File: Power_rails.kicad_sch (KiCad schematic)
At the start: 73 parts

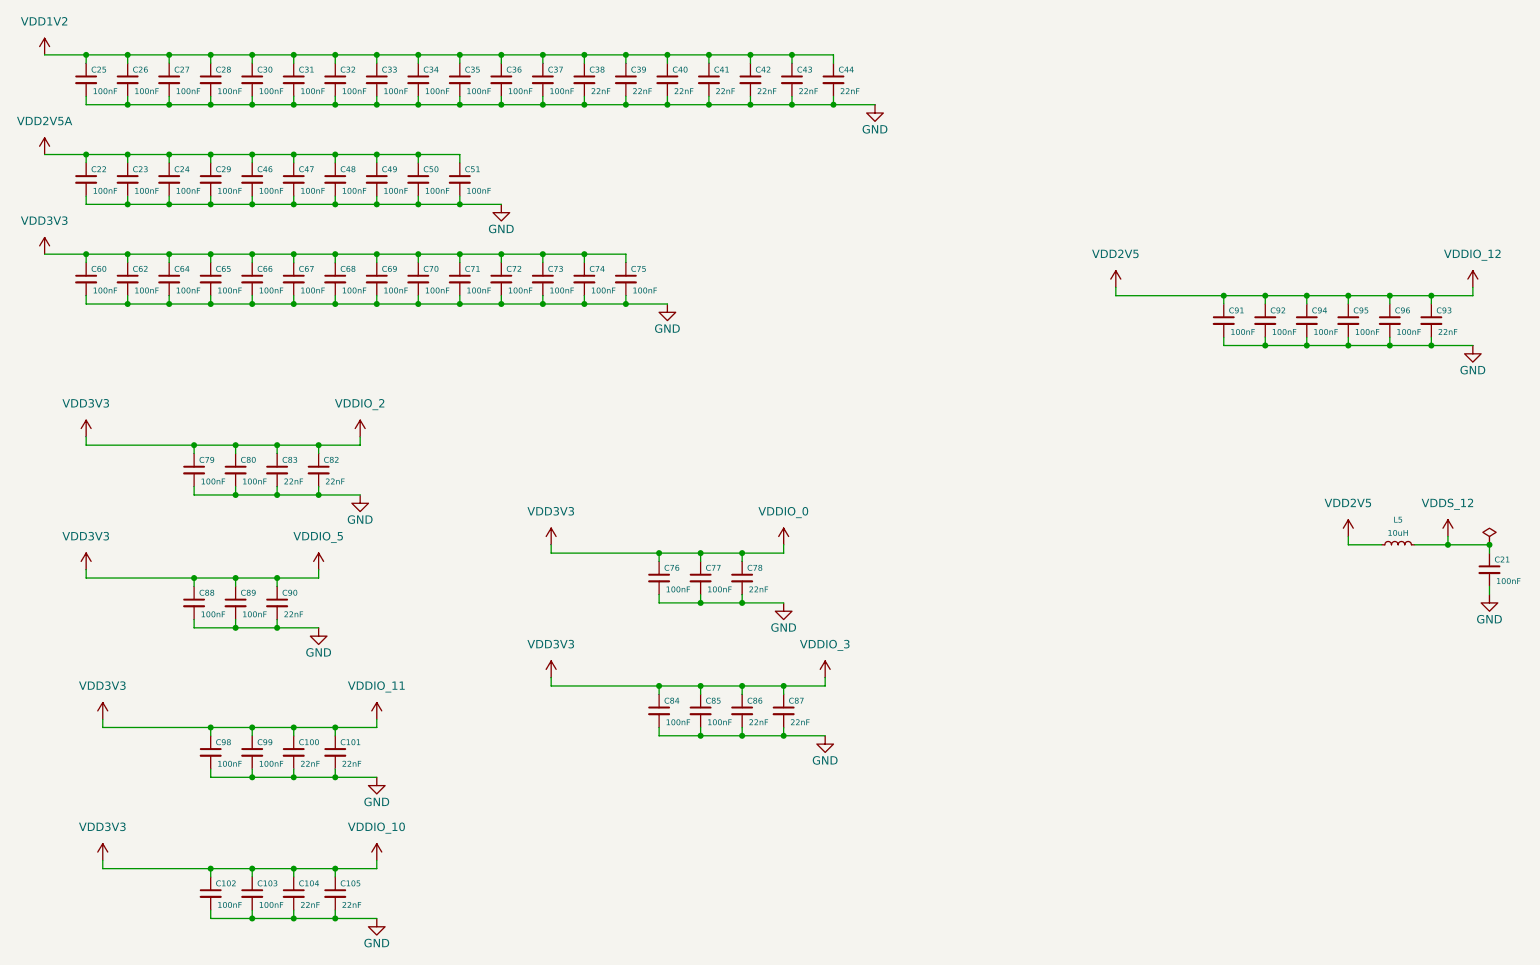
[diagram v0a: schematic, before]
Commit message: pre-order adjustments
DF9 connectors footprint adjusted.
Dimensions of board edges changed.
Placement of DF9 adjusted.
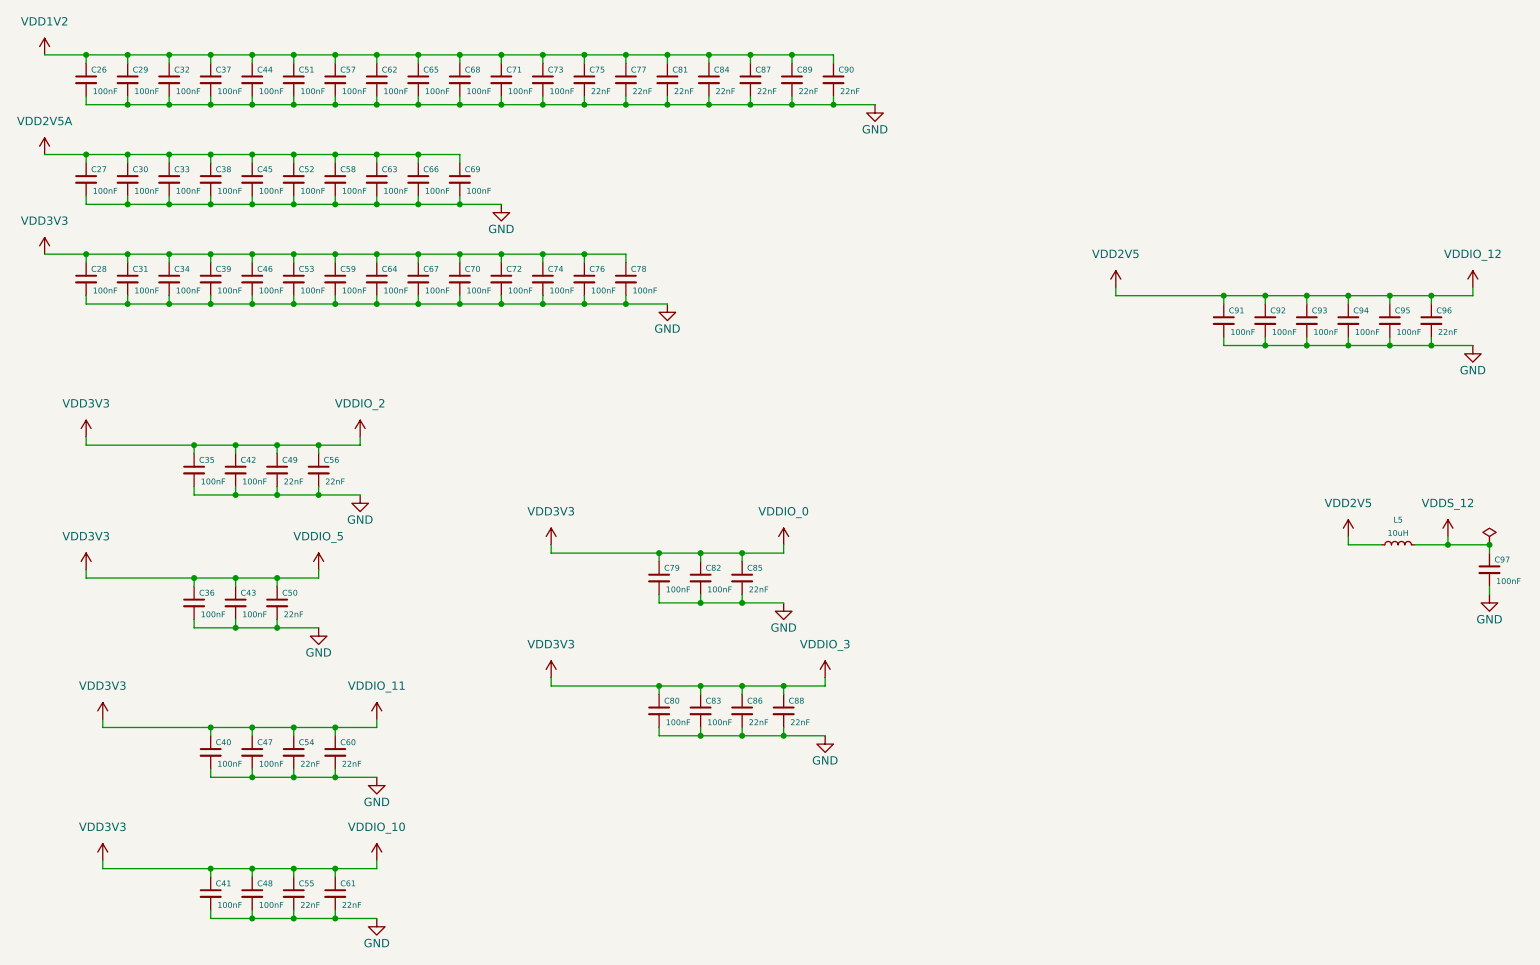
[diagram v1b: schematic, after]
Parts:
- renumbered C25 to C26, C22 to C27, C60 to C28, C26 to C29, C23 to C30, C62 to C31, C27 to C32, C24 to C33, C64 to C34, C79 to C35, C88 to C36, C28 to C37, C29 to C38, C65 to C39, C98 to C40, C102 to C41, C80 to C42, C89 to C43, C30 to C44, C46 to C45, C66 to C46, C99 to C47, C103 to C48, C83 to C49, C90 to C50, C31 to C51, C47 to C52, C67 to C53, C100 to C54, C104 to C55, C82 to C56, C32 to C57, C48 to C58, C68 to C59, C101 to C60, C105 to C61, C33 to C62, C49 to C63, C69 to C64, C34 to C65, C50 to C66, C70 to C67, C35 to C68, C51 to C69, C71 to C70, C36 to C71, C37 to C73, C73 to C74, C38 to C75, C74 to C76, C39 to C77, C75 to C78, C76 to C79, C84 to C80, C40 to C81, C77 to C82, C85 to C83, C41 to C84, C78 to C85, C42 to C87, C87 to C88, C43 to C89, C44 to C90, C94 to C93, C95 to C94, C96 to C95, C93 to C96, C21 to C97

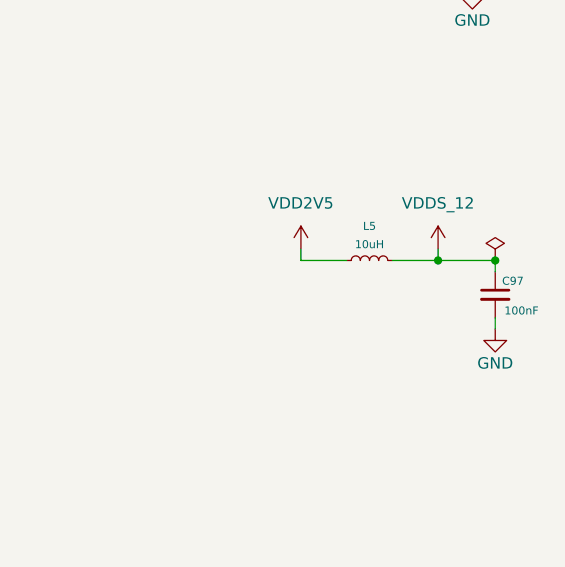
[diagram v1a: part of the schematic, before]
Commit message: pre order adjustments. Board symmetry
adjusted little things brought up by DFM checker of JLCPCB. Board's edges fully symmetrical on y axis. 2mm shift on x axis of the DF9s maintained
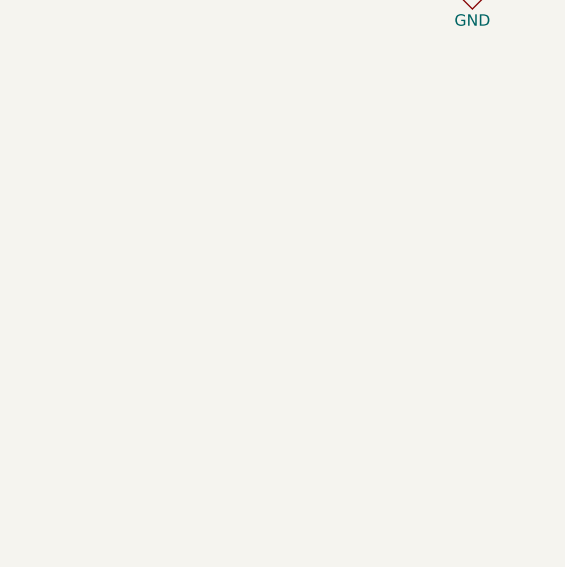
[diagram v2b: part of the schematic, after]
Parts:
- removed C97: 100nF, Capacitor_SMD:C_0402_1005Metric_Pad0.74x0.62mm_HandSolder, symbol Device:C_Small
- removed L5: 10uH, Inductor_SMD:L_0402_1005Metric_Pad0.77x0.64mm_HandSolder, symbol Device:L_Small

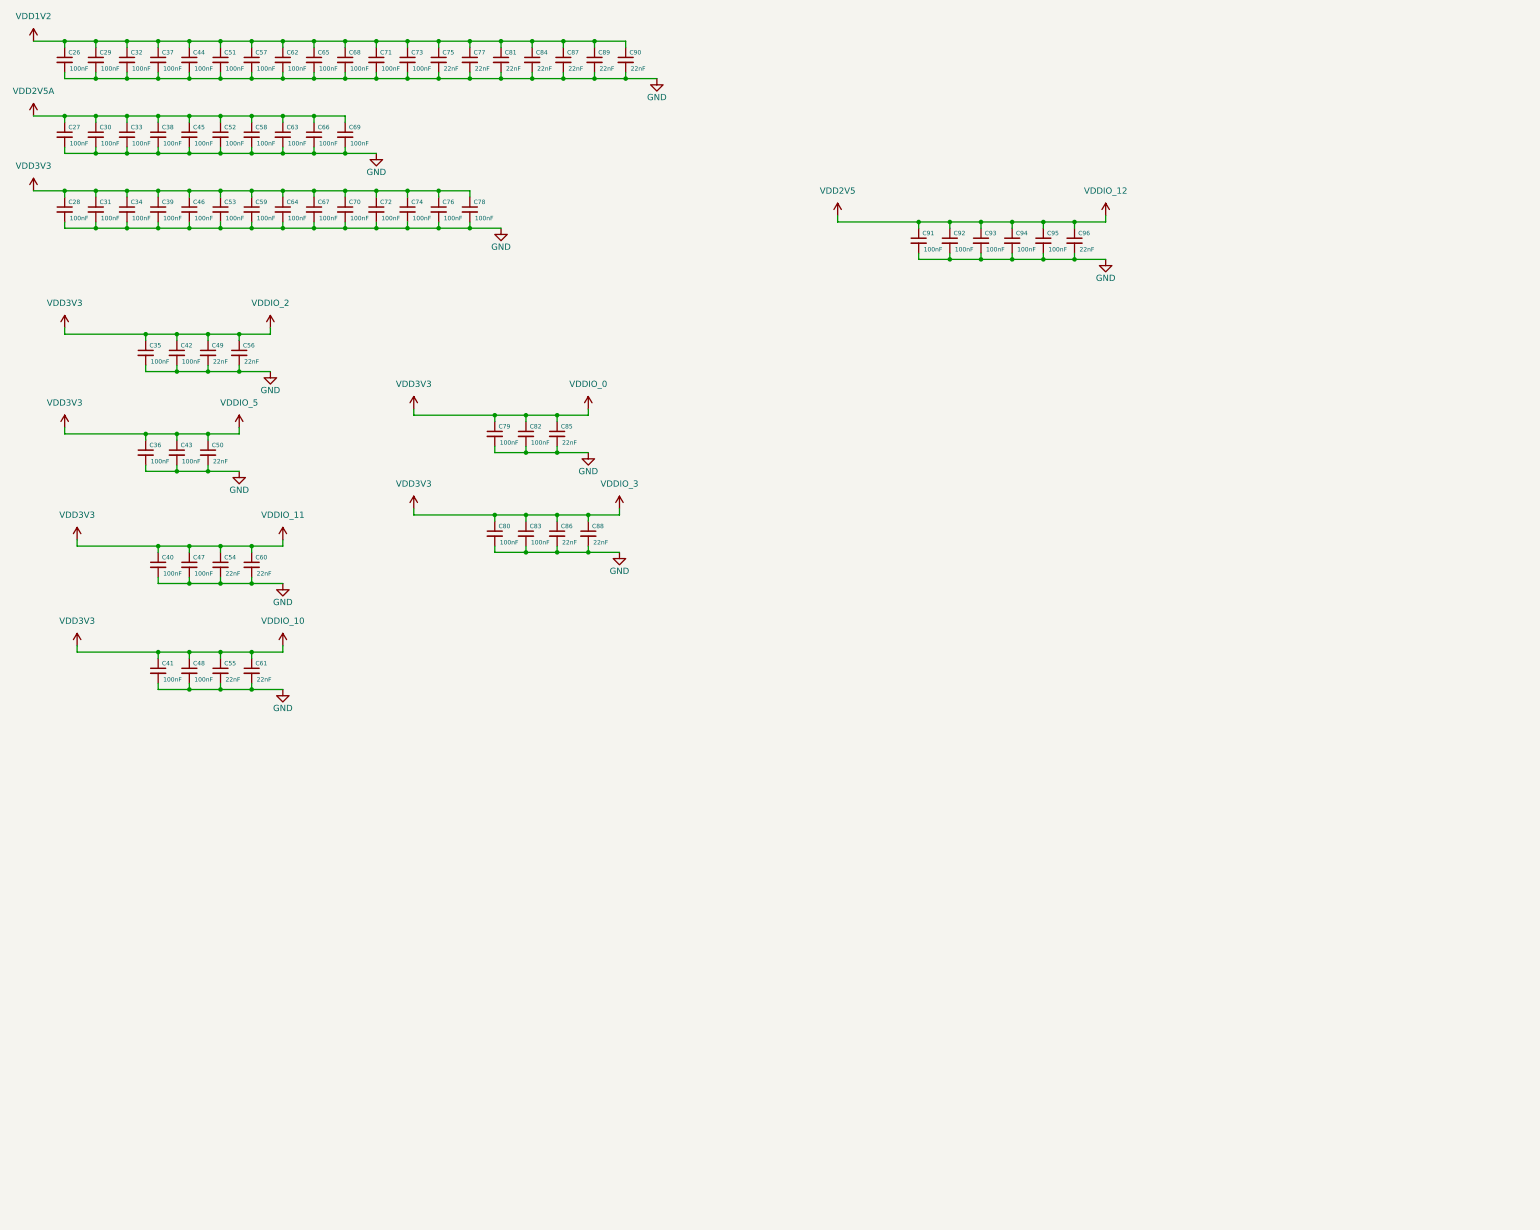
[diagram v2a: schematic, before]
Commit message: added extra decoupling capacitors
extra decoupling on 2V5IO and Service rails
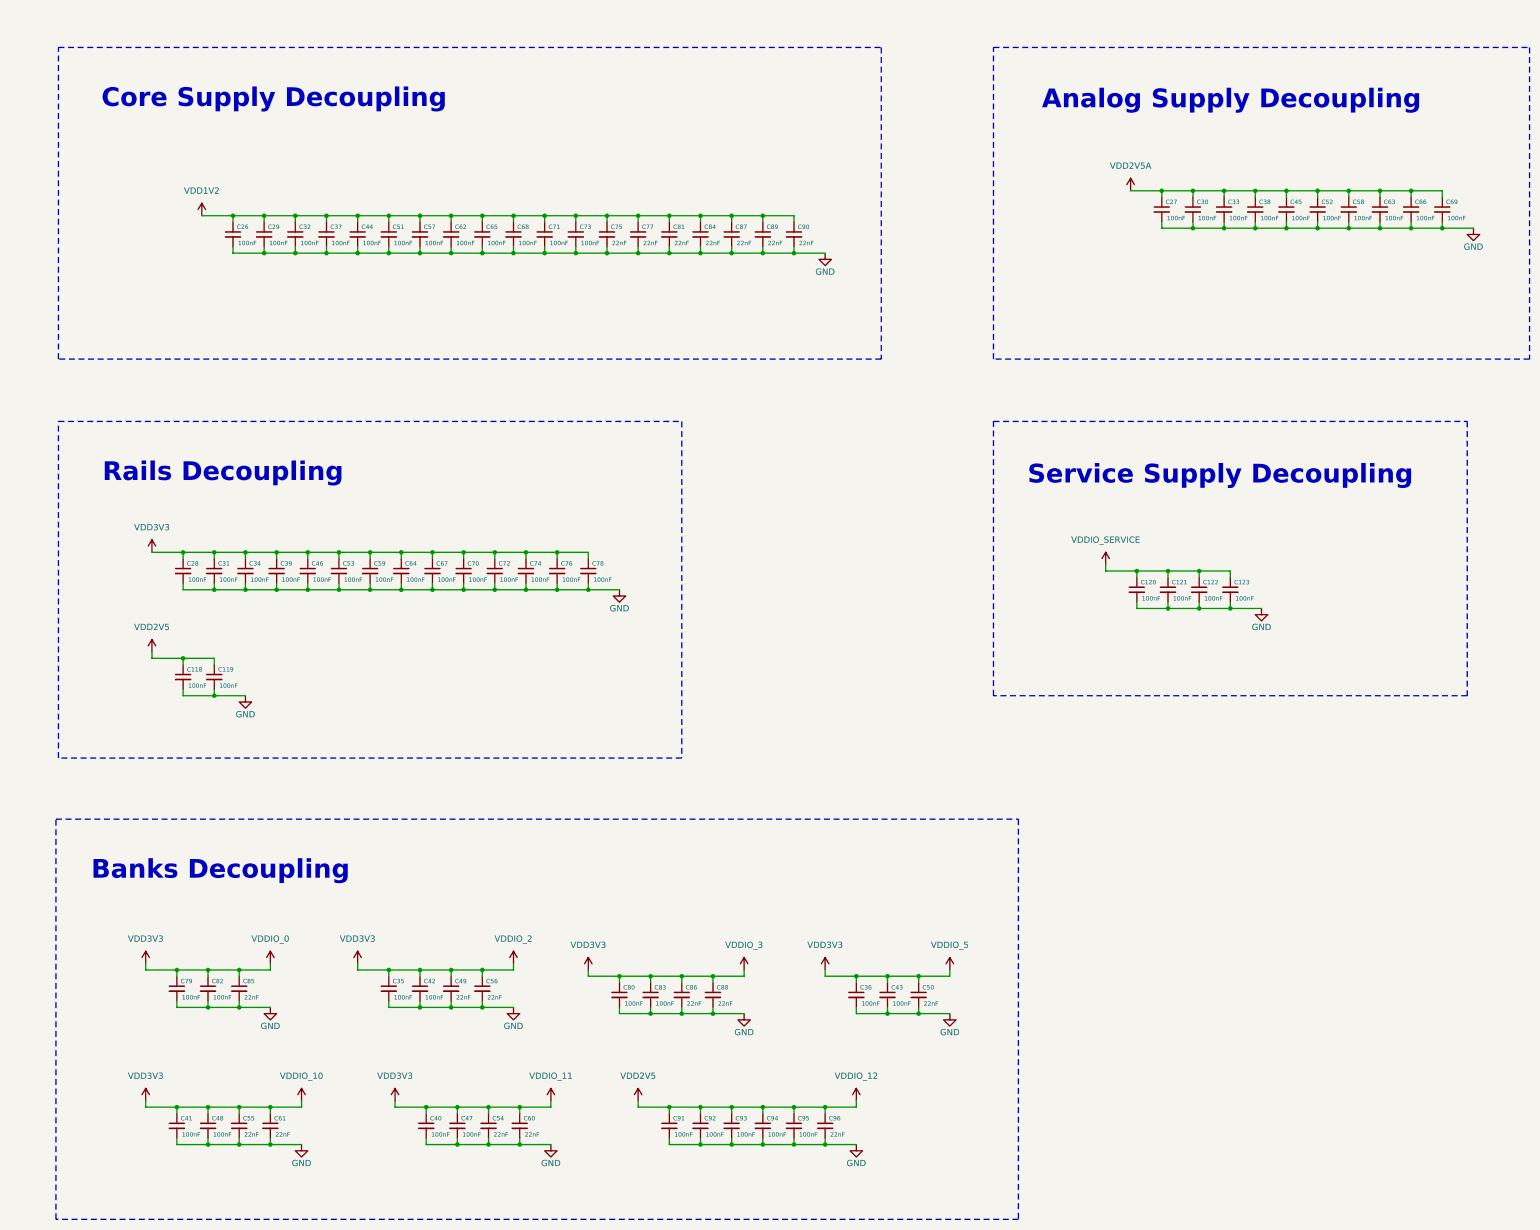
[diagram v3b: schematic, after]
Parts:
- added C118, C119, C120, C121, C122, C123: 100nF, Capacitor_SMD:C_0402_1005Metric_Pad0.74x0.62mm_HandSolder, symbol Device:C_Small
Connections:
- net GND: now also C118.2, C119.2, C120.2, C121.2, C122.2, C123.2
- net VDD2V5: now also C118.1, C119.1
- new net VDDIO_SERVICE: C120.1, C121.1, C122.1, C123.1
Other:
- note added: "Analog Supply Decoupling"
- note added: "Banks Decoupling"
- note added: "Core Supply Decoupling"
- note added: "Rails Decoupling"
- note added: "Service Supply Decoupling"
- moved on the sheet: C26, C27, C28, C29, C30, C31, C32, C33, C34, C35, C36, C37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
